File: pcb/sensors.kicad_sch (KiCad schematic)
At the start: 11 parts, among them J10 RG-9/11/15, J11 RJ12 (rain), J12 RJ12 (wind), U7 SRV05-4, U8 SRV05-4

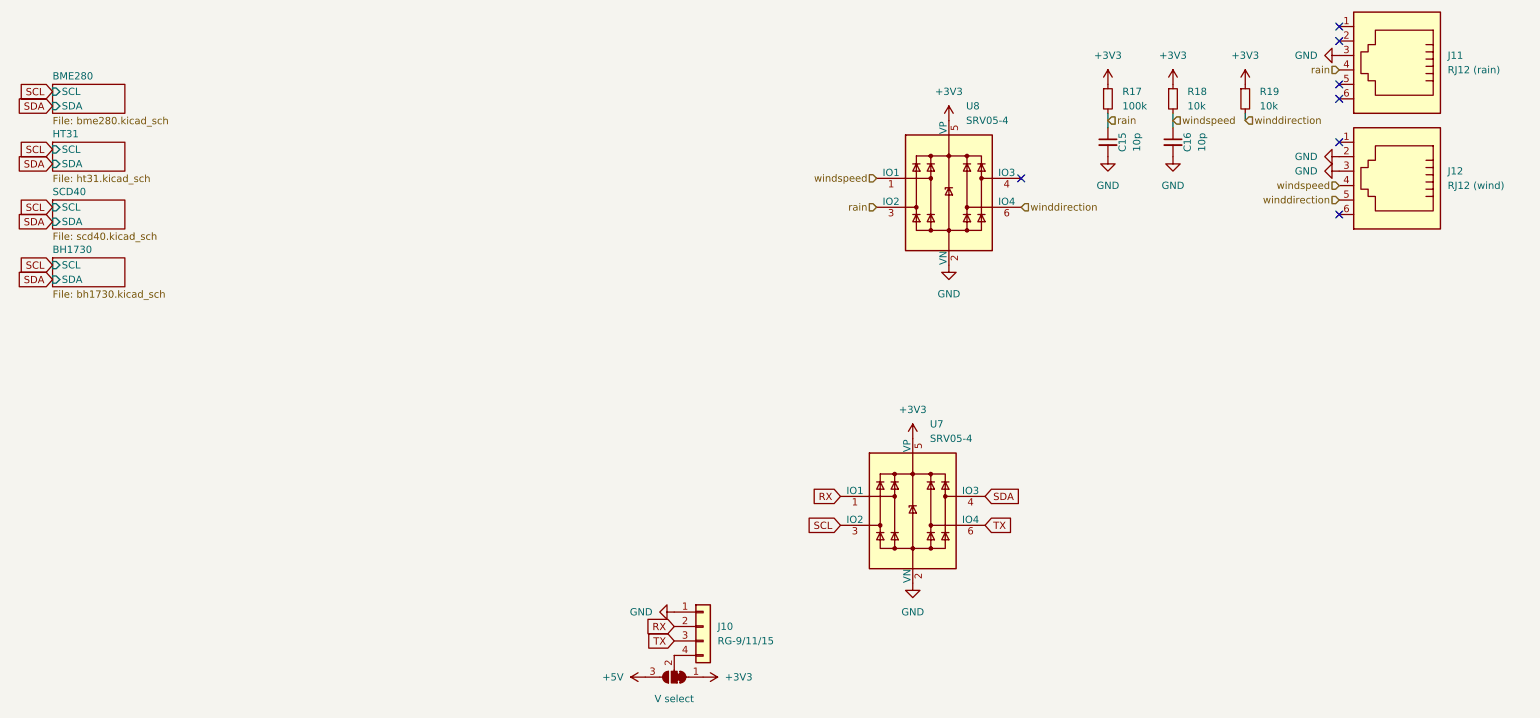
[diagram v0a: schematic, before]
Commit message: Rename pcb, add sensors and fix some issues
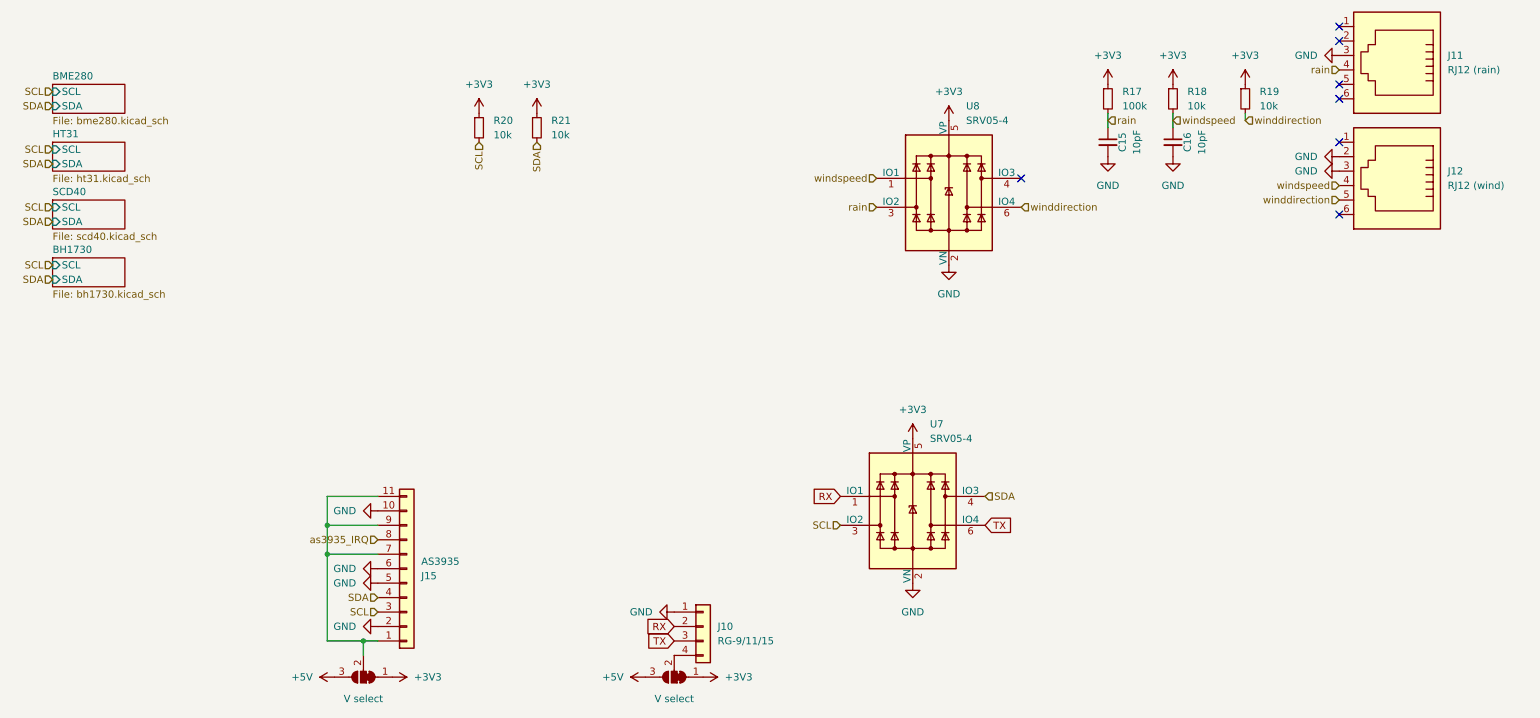
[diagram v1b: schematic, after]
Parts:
- added J15: AS3935, Connector_PinSocket_2.54mm:PinSocket_1x11_P2.54mm_Vertical, symbol Connector_Generic:Conn_01x11
- added JP6: V select, Jumper:SolderJumper-3_P1.3mm_Bridged12_RoundedPad1.0x1.5mm, symbol Jumper:SolderJumper_3_Bridged12
- added R20, R21: 10k, Resistor_SMD:R_0603_1608Metric, symbol Device:R_Small
- C15, C16: value 10p -> 10pF
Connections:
- net +3V3: now also JP6.1 (A), R20.1, R21.1
- net +5V: now also JP6.3 (B)
- net GND: now also J15.10 (Pin_10), J15.2 (Pin_2), J15.5 (Pin_5), J15.6 (Pin_6)
- net SCL: now also J15.3 (Pin_3), R20.2
- net SDA: now also J15.4 (Pin_4), R21.2
- new net: J15.1 (Pin_1), J15.11 (Pin_11), J15.7 (Pin_7), J15.9 (Pin_9), JP6.2 (C)
- new net as3935_IRQ: J15.8 (Pin_8)
